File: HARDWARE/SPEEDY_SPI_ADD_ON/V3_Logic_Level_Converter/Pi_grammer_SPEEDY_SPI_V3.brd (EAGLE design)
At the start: 25.4 x 61 mm, 12 parts, among them J2 TARGET_copy

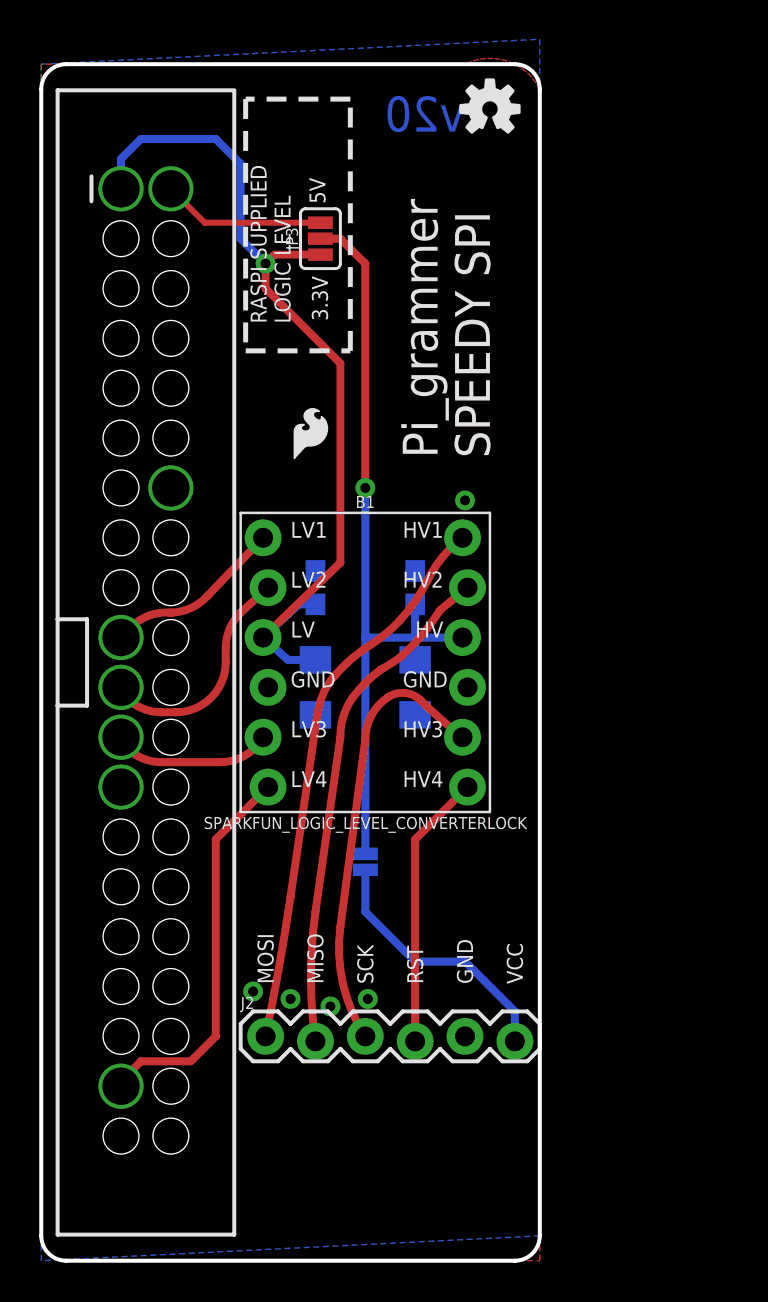
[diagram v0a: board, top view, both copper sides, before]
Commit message: Speedy SPI corrections
Extended out to the right, and scooted all components to clear current
Pi_grammer "hat" design.

On V2, I had to solder all of the PTH pins flush on the bottom, and the
SMD parts below the LLC get in the way.
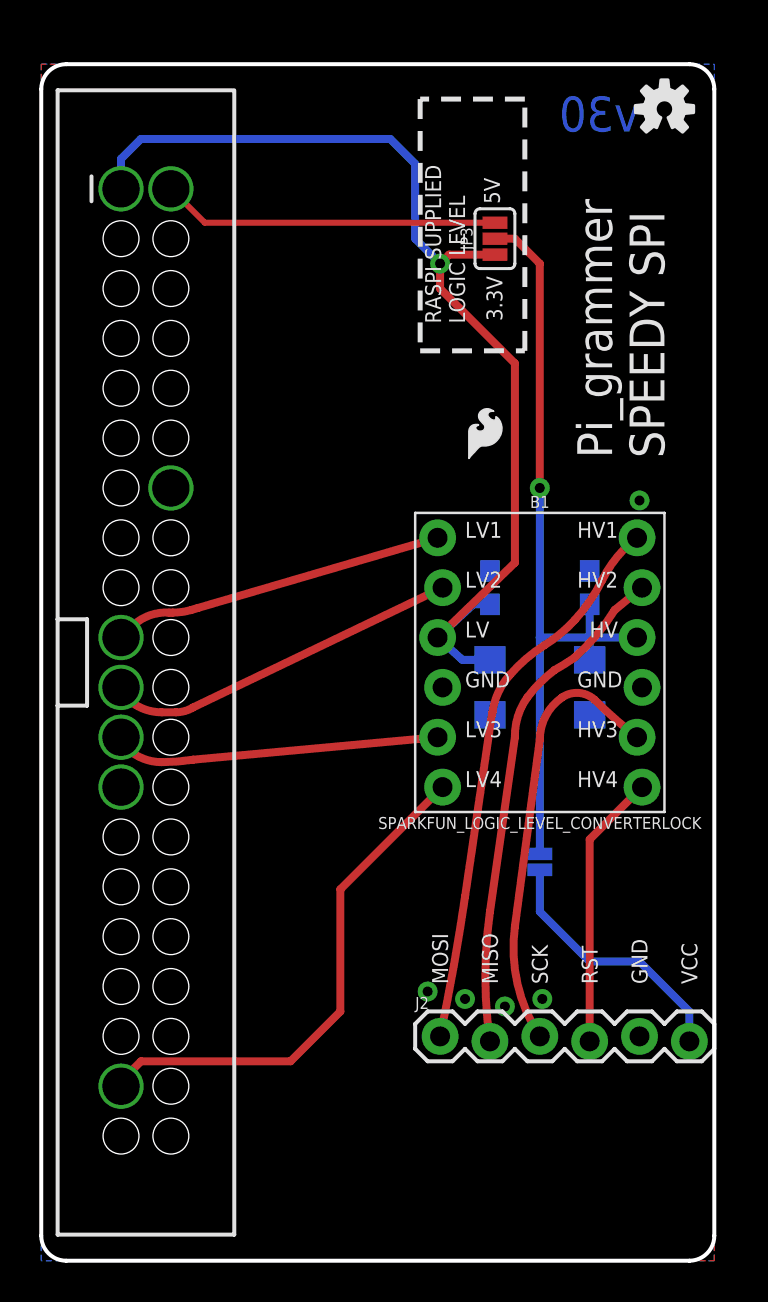
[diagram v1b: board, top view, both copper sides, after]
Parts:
- moved C3 8.89 mm to (67.3, 49.5)
- moved C4 8.89 mm to (72.4, 49.5)
- moved C5 8.89 mm to (72.4, 44.5)
- moved C6 8.89 mm to (67.3, 44.5)
- moved LOGO2 8.89 mm to (76.2, 73.9)
- moved B1 8.89 mm to (69.8, 45.7)
- moved J2 8.89 mm to (64.8, 26.7)
- moved JP1 8.89 mm to (69.8, 35.6)
- moved JP3 8.89 mm to (67.6, 67.3)
- moved LOGO1 8.89 mm to (65.9, 55.8)
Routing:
- net 3.3V: track 45.9 -> 54.8 mm
- net 5V: track 8.34 -> 17.2 mm
- net SCLK: track 8.16 -> 16.7 mm
- net MOSI: track 9.07 -> 17.0 mm
- net MISO: track 11.5 -> 18.3 mm
- net RST: track 19.8 -> 26.5 mm
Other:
- board size 25.4 x 61 mm -> 34.3 x 61 mm
- board text added: "v30"
- board text removed: "v20"
